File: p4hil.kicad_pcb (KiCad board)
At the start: 4 copper layers, 81.3 x 50.8 mm, 216 parts, among them J1 Conn_02x02_Odd_Even, J10 Conn_01x20, J11 Conn_01x20, J12 Conn_01x20, J13 USB_A_Stacked, J14 Conn_01x04, J15 Conn_01x20, J16 Conn_01x04, J17 Barrel_Jack_Switch, J18 Conn_02x05_Odd_Even, J19 HR871150C, J2 Conn_01x08, J3 USB_C_Receptacle_USB2.0_16P, J4 Conn_01x10, J5 Conn_01x20, J6 Conn_01x20, J7 Conn_01x20, J8 Conn_01x02, J9 Conn_01x06, SW1 SW_Push, SW2 SW_Push, U1 W25Q128JVS, U10 TLV62569DBV, U11 MT9700_SY6280, U3 TLV62569DBV, U4 IPGRI, U6 INA219AxD, U7 CH334F, U8 MT9700_SY6280, U9 MT9700_SY6280, Y1 40MHz(+-10 ppm) C501798, Y2 25Mhz 12pf, Y3 12MHz

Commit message: Swirly gridify
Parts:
- removed R93: 2.2K, Resistor_SMD:R_0402_1005Metric
- added REF**: MountingHole_2.5mm, MountingHole:MountingHole_2.5mm, F.Cu at (177.8, 125.4)
- added REF**: MountingHole_2.5mm, MountingHole:MountingHole_2.5mm, F.Cu at (106.7, 69.5)
- added REF**: MountingHole_2.5mm, MountingHole:MountingHole_2.5mm, F.Cu at (177.8, 69.5)
- added REF**: MountingHole_2.5mm, MountingHole:MountingHole_2.5mm, F.Cu at (106.7, 125.4)
- J10, J11, J12, J15, J6, J7: footprint Connector_PinHeader_2.54mm:PinHeader_1x20_P2.54mm_Vertical -> Connector_PinHeader_2.54mm:PinHeader_1x19_P2.54mm_Vertical
- moved C54 12.3 mm to (182.4, 92.4)
- moved D1 12.3 mm to (184.4, 92.5)
- moved J1 11.8 mm to (165.1, 98.8)
- moved J17 2.81 mm to (176.4, 117.9)
- moved J3 2.81 mm to (182.4, 100.0)
- moved JP3 2.79 mm to (174.0, 103.8), turned to -90 degrees
- moved J10 2.55 mm to (114.3, 100.0)
- moved J11 2.55 mm to (114.3, 105.1)
- moved J12 2.55 mm to (114.3, 95.0)
- moved J15 2.55 mm to (114.3, 107.7)
- moved J6 2.55 mm to (114.3, 97.5)
- moved J7 2.55 mm to (114.3, 102.6)
- moved R85 2.54 mm to (142.2, 110.4)
- moved R88 2.54 mm to (149.9, 110.4)
- moved R92 2.54 mm to (160.0, 110.4)
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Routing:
- net /DeviceUnderTest/T9i: track 0.00 -> 15.0 mm
- net /DeviceUnderTest/T8i: track 0.00 -> 15.0 mm
- net /DeviceUnderTest/T7i: track 0.00 -> 15.0 mm
- net /DeviceUnderTest/T6i: track 0.00 -> 15.0 mm
- net /DeviceUnderTest/T5i: track 0.00 -> 15.0 mm
- net /DeviceUnderTest/T4i: track 0.00 -> 15.0 mm
- net /DeviceUnderTest/T3i: track 0.00 -> 15.0 mm
- net /DeviceUnderTest/T2i: track 0.00 -> 15.0 mm
- net /DeviceUnderTest/T1i: track 0.00 -> 15.0 mm
- net /DeviceUnderTest/T19i: track 0.00 -> 15.0 mm
- net /DeviceUnderTest/T18i: track 0.00 -> 15.0 mm
- net /DeviceUnderTest/T17i: track 0.00 -> 15.0 mm
- net /DeviceUnderTest/T16i: track 0.00 -> 15.0 mm
- net /DeviceUnderTest/T15i: track 0.00 -> 15.0 mm
- net /DeviceUnderTest/T14i: track 0.00 -> 15.0 mm
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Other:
- board size 81.3 x 50.8 mm -> 81.3 x 61 mm
- board text added: "0.5{dblquote}"
- board text added: "0.6{dblquote}"
- board text added: "0.7{dblquote}"
- board text added: "0.8{dblquote}"
- board text added: "0.9{dblquote}"
- board text added: "1.0{dblquote}"
- board text added: "5+x4 swirly grid squares"

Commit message: more routing
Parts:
- C35, C36, C37, C38, C39, C40, R10: moved to F.Cu
- C41, C42, C46, C47, C48, R11, R12, R13, R32, U4, Y2: moved to B.Cu
- R50: value R_Protect -> 1.5k; moved to B.Cu
- moved R34 11.8 mm to (182.3, 72.5)
- moved R13 10.9 mm to (162.4, 78.1), turned to -90 degrees
- moved R32 10.9 mm to (163.4, 78.1), turned to -90 degrees
- moved J18 10.5 mm to (125.7, 79.1), turned to -90 degrees
- moved C41 9.25 mm to (166.7, 87.9), turned to 90 degrees
- moved C42 9.25 mm to (161.4, 87.9), turned to -90 degrees
- moved Y2 9.25 mm to (164.1, 87.9)
- moved C43 8.31 mm to (167.7, 83.3), turned to -90 degrees
- moved C37 7.27 mm to (162.4, 82.3), turned to 0 degrees
- moved R11 7.21 mm to (166.9, 80.0)
- moved R50 7.08 mm to (164.5, 78.1), turned to -90 degrees
- moved SW2 6.78 mm to (105.9, 103.5), turned to -90 degrees
- moved PORT4 5.71 mm to (107.1, 99.6)
- moved R12 4.98 mm to (165.7, 85.6)
- moved C38 4.95 mm to (161.5, 83.6), turned to 0 degrees
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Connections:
- J1 pad 2: /Ethernet/POWER2 -> /Ethernet/POWER1
- J1 pad 3: /Ethernet/POWER1 -> /Ethernet/POWER2
- J2 pad 1: /DeviceUnderTest/T13i -> /DeviceUnderTest/T12i
- J2 pad 2: /DeviceUnderTest/T14i -> /DeviceUnderTest/T13i
- J2 pad 3: /DeviceUnderTest/T15i -> /DeviceUnderTest/T14i
- J2 pad 4: /DeviceUnderTest/T16i -> /DeviceUnderTest/T15i
- J2 pad 5: /DeviceUnderTest/T17i -> /DeviceUnderTest/T16i
- J2 pad 6: /DeviceUnderTest/T18i -> /DeviceUnderTest/T17i
- J2 pad 7: /DeviceUnderTest/T19i -> /DeviceUnderTest/T18i
- J2 pad 8: /DeviceUnderTest/T20i -> /DeviceUnderTest/T19i
- J4 pad 10: /DeviceUnderTest/T10i -> /DeviceUnderTest/T9i
- J4 pad 4: /DeviceUnderTest/T4i -> unconnected-(J4-Pin_4-Pad4)
- J4 pad 5: /DeviceUnderTest/T5i -> /DeviceUnderTest/T4i
- J4 pad 6: /DeviceUnderTest/T6i -> /DeviceUnderTest/T5i
- J4 pad 7: /DeviceUnderTest/T7i -> /DeviceUnderTest/T6i
- J4 pad 8: /DeviceUnderTest/T8i -> /DeviceUnderTest/T7i
- J4 pad 9: /DeviceUnderTest/T9i -> /DeviceUnderTest/T8i
- J8 pad 1: /T11 -> /DeviceUnderTest/T10i
- J8 pad 2: /T12 -> /DeviceUnderTest/T11i
- R50 pad 1: /DeviceUnderTest/T20i -> +3.3V
- R50 pad 2: /T20 -> /MDIO
- U2 pad 10: /T6 -> /T4
- U2 pad 11: /T5 -> /T3
- U2 pad 12: /T4 -> /T2
- U2 pad 13: /T3 -> /T1
- U2 pad 14: /T2 -> /P4/GPIO13/ADC
- U2 pad 15: /T1 -> /B1
- U2 pad 16: /P4/GPIO15/ADC -> /B2
- U2 pad 17: /P4/GPIO16/ADC -> /B3
- U2 pad 18: /P4/GPIO17/ADC -> /B4
- U2 pad 19: /P4/GPIO18/ADC -> /B5
- U2 pad 20: /P4/GPIO19/ADC -> /B6
- U2 pad 22: /P4/GPIO20/ADC -> /B7
- U2 pad 23: /P4/GPIO21/ADC -> /B8
- U2 pad 24: /P4/GPIO22/ADC -> /B9
- U2 pad 25: /P4/GPIO23/ADC -> /B10
- U2 pad 3: /T12 -> /T10
- U2 pad 4: /T11 -> /T9
- U2 pad 5: /T10 -> /T8
- U2 pad 55: /P4/GPIO26/ADC/USB -> /B11
- U2 pad 56: /P4/GPIO27/ADC/USB -> /B12
- U2 pad 57: /P4/GPIO28 -> /B13
- U2 pad 58: /P4/GPIO29 -> /B14
- U2 pad 6: /T9 -> /T7
- U2 pad 60: /P4/GPIO30 -> /T11
- U2 pad 61: /P4/GPIO31 -> /T12
- U2 pad 63: /P4/GPIO32 -> /B15
- U2 pad 64: /P4/GPIO33 -> /B16
- U2 pad 65: /P4/GPIO34 -> /B17
- U2 pad 69: /P4/GPIO37/UART0_TXD -> /B18
- U2 pad 7: /T8 -> /T6
- U2 pad 70: /P4/GPIO38/UART0_RXD -> /B19
- U2 pad 8: /T7 -> /T5
- U2 pad 80: /P4/GPIO39 -> /B20
- U2 pad 92: /T20 -> /PHY_RESETN
- U4 pad 32: /Ethernet/PHY_RESET -> /PHY_RESETN
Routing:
- net +3.3V: track 51.3 -> 180.9 mm, vias 8 -> 13
- net /DeviceUnderTest/I2C_PULL_UP: track 0.00 -> 115.9 mm
- net +5V: track 0.00 -> 107.5 mm
- net /NEOPIXEL_WAKE: track 0.00 -> 61.6 mm, vias 0 -> 1
- net /USB_SERIAL-: track 0.00 -> 55.9 mm, vias 0 -> 4
- net /USB_SERIAL+: track 0.00 -> 55.1 mm, vias 0 -> 2
- net /DeviceUnderTest/B1i: track 3.72 -> 55.9 mm
- net /B20: track 0.00 -> 47.3 mm, vias 0 -> 4
- net /DeviceUnderTest/B2i: track 0.00 -> 46.5 mm
- net /USB Host/USB_VBUS: track 0.00 -> 41.8 mm
- net /DeviceUnderTest/B3i: track 0.00 -> 40.7 mm
- net /MDIO: track 0.00 -> 38.3 mm, vias 0 -> 3
- net /DeviceUnderTest/B4i: track 0.00 -> 35.3 mm
- net /PHY_RESETN: track 0.00 -> 32.1 mm, vias 0 -> 2
- net /DeviceUnderTest/B5i: track 0.00 -> 29.9 mm
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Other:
- board text added: "+V"
- board text added: "1"
- board text added: "2"
- board text added: "3"
- board text added: "4"
- board text added: "45"
- board text added: "5V"
- board text added: "78"
- board text added: "A"
- board text added: "G"
- board text added: "USB"

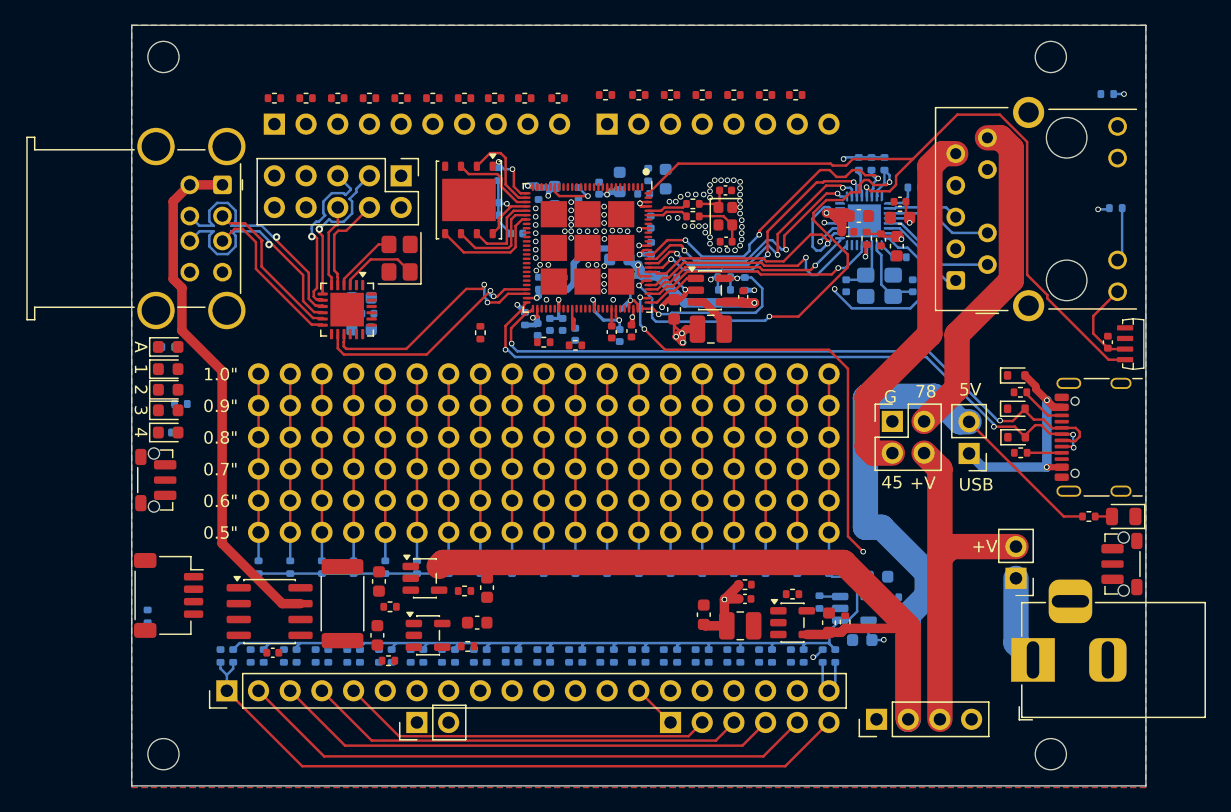
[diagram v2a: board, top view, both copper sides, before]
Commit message: Lots more routing
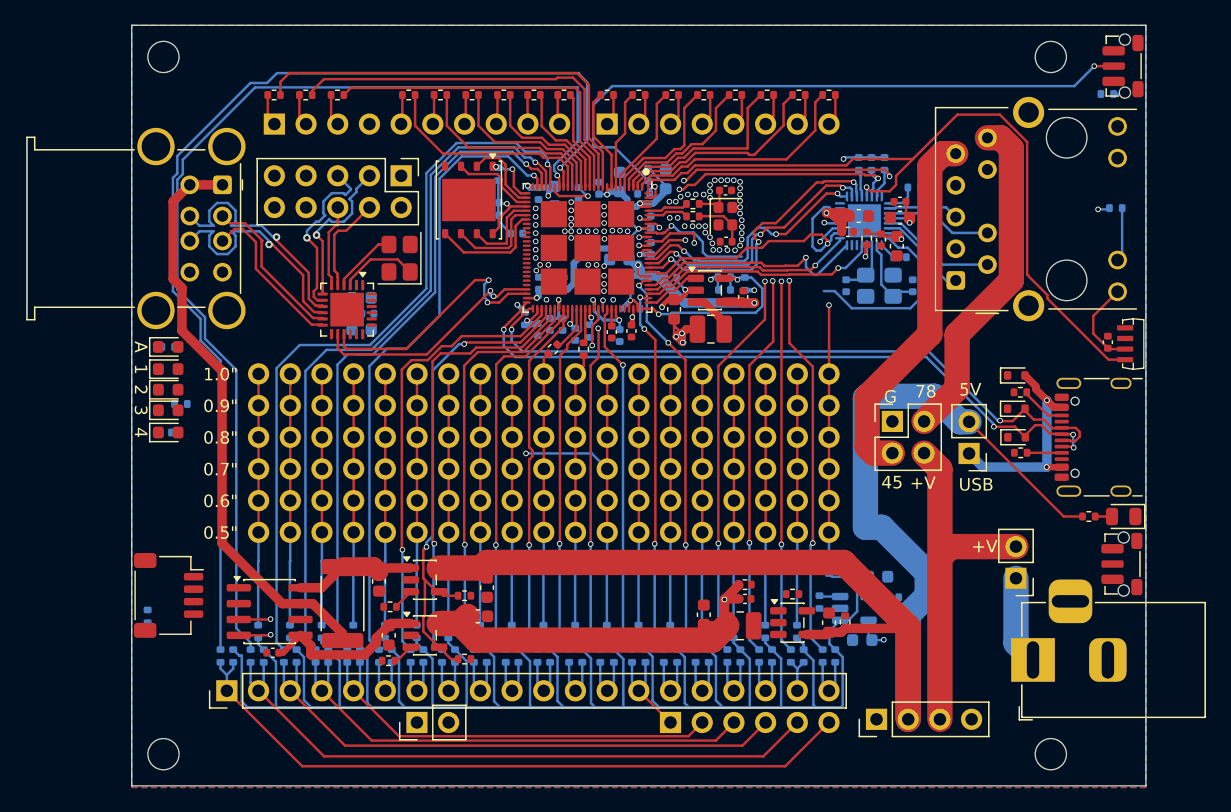
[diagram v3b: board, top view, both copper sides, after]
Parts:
- R24: moved to B.Cu
- moved SW2 84.6 mm to (183.7, 70.3), turned to 90 degrees
- moved R42 20.2 mm to (142.2, 72.6), turned to 180 degrees
- moved R40 20.1 mm to (137.9, 93.0), turned to 45 degrees
- moved R24 8.74 mm to (140.8, 91.5)
- moved R74 5.16 mm to (114.3, 115.6)
- moved R75 5.16 mm to (116.8, 115.6)
- moved R76 5.16 mm to (119.4, 115.6)
- moved R77 5.16 mm to (121.9, 115.6)
- moved R78 5.16 mm to (124.4, 115.6)
- moved R79 5.16 mm to (127.0, 115.6)
- moved R80 5.16 mm to (129.5, 115.6)
- moved R81 5.16 mm to (132.1, 115.6)
- moved R82 5.16 mm to (134.6, 115.6)
- moved R83 5.16 mm to (137.1, 115.6)
- moved R84 5.16 mm to (139.7, 115.6)
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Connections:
- R22 pad 1: /USB Host/POWER_ON -> /USB_POWER_ON
- R23 pad 1: /USB Host/POWER_ON -> /USB_POWER_ON
- U2 pad 1: /T14 -> /T19
- U2 pad 10: /T4 -> /T1
- U2 pad 11: /T3 -> /T2
- U2 pad 12: /T2 -> /T3
- U2 pad 13: /T1 -> /T9
- U2 pad 14: /P4/GPIO13/ADC -> /T8
- U2 pad 15: /B1 -> /T7
- U2 pad 16: /B2 -> /T6
- U2 pad 17: /B3 -> /T5
- U2 pad 18: /B4 -> /T4
- U2 pad 19: /B5 -> /B1
- U2 pad 2: /T13 -> /T18
- U2 pad 20: /B6 -> /B2
- U2 pad 22: /B7 -> /B3
- U2 pad 23: /B8 -> /B4
- U2 pad 24: /B9 -> /B5
- U2 pad 25: /B10 -> /B6
- U2 pad 3: /T10 -> /T17
- U2 pad 4: /T9 -> /T16
- U2 pad 5: /T8 -> /T15
- U2 pad 55: /B11 -> /B7
- U2 pad 56: /B12 -> /USB_POWER_ON
- U2 pad 57: /B13 -> /B8
- U2 pad 58: /B14 -> /B9
- U2 pad 6: /T7 -> /T14
- U2 pad 60: /T11 -> /B10
- U2 pad 61: /T12 -> /B11
- U2 pad 63: /B15 -> /T10
- U2 pad 64: /B16 -> /B12
- U2 pad 65: /B17 -> /T11
- U2 pad 69: /B18 -> /B13
- U2 pad 7: /T6 -> /T13
- U2 pad 70: /B19 -> /B14
- U2 pad 8: /T5 -> /T12
- U2 pad 80: /B20 -> /B15
- U2 pad 84: /MDIO -> /B16
- U2 pad 90: /MDC -> /B19
- U2 pad 92: /PHY_RESETN -> /B17
- U2 pad 93: /T19 -> /B20
- U2 pad 94: /T18 -> /B18
- U2 pad 95: /T17 -> /PHY_RESETN
- U2 pad 97: /T16 -> /MDC
- U2 pad 98: /T15 -> /MDIO
- U8 pad 4: /USB Host/POWER_ON -> /USB_POWER_ON
- U9 pad 4: /USB Host/POWER_ON -> /USB_POWER_ON
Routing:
- net /B1: track 0.00 -> 86.6 mm, vias 0 -> 1
- net /B2: track 0.00 -> 84.9 mm, vias 0 -> 1
- net /DeviceUnderTest/I2C_PULL_UP: track 115.9 -> 180.3 mm
- net /B3: track 0.00 -> 60.3 mm, vias 0 -> 1
- net /B4: track 0.00 -> 56.8 mm, vias 0 -> 1
- net /RESET: track 0.17 -> 54.9 mm, vias 0 -> 2
- net /B5: track 0.00 -> 53.8 mm, vias 0 -> 1
- net /SCL: track 0.00 -> 52.2 mm, vias 0 -> 2
- net /DeviceUnderTest/T12i: track 15.0 -> 66.4 mm, vias 0 -> 1
- net /B6: track 0.00 -> 51.3 mm, vias 0 -> 1
- net /SDA_BOOT: track 0.00 -> 51.2 mm, vias 0 -> 2
- net /B18: track 0.00 -> 43.6 mm, vias 0 -> 3
- net /B17: track 0.00 -> 43.4 mm, vias 0 -> 3
- net /B19: track 0.00 -> 42.5 mm, vias 0 -> 3
- net /USB_POWER_ON: track 0.00 -> 39.8 mm, vias 0 -> 2
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
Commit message: close to routed
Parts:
- R25: moved to F.Cu
- moved R25 5.27 mm to (110.1, 116.9), turned to -90 degrees
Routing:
- net /DeviceUnderTest/T13i: track 22.7 -> 61.5 mm, vias 0 -> 1
- net /DeviceUnderTest/T14i: track 22.7 -> 58.8 mm, vias 0 -> 1
- net /USB Host/SWITCHED_3V3: track 13.5 -> 47.3 mm, vias 0 -> 4
- net +3.3V: track 219.2 -> 252.1 mm, vias 14 -> 17
- net /USB Host/LED4: track 0.00 -> 32.8 mm, vias 0 -> 4
- net /USB Host/LED1: track 0.00 -> 28.0 mm, vias 0 -> 2
- net /DeviceUnderTest/T15i: track 22.7 -> 50.7 mm, vias 0 -> 1
- net /DeviceUnderTest/T16i: track 22.7 -> 47.4 mm, vias 0 -> 1
- net /DeviceUnderTest/T17i: track 22.7 -> 45.1 mm, vias 0 -> 1
- net /USB Host/SWITCHED_5V: track 9.83 -> 31.8 mm, vias 0 -> 2
- net /DeviceUnderTest/T18i: track 22.7 -> 43.7 mm, vias 0 -> 1
- net /USB Host/LED2: track 0.00 -> 20.1 mm, vias 0 -> 4
- net /USB Host/USB_VBUS: track 46.7 -> 65.1 mm
- net /PHY_RESETN: track 24.2 -> 35.2 mm, vias 1 -> 3
- net Net-(U10-FB): track 0.00 -> 6.88 mm
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
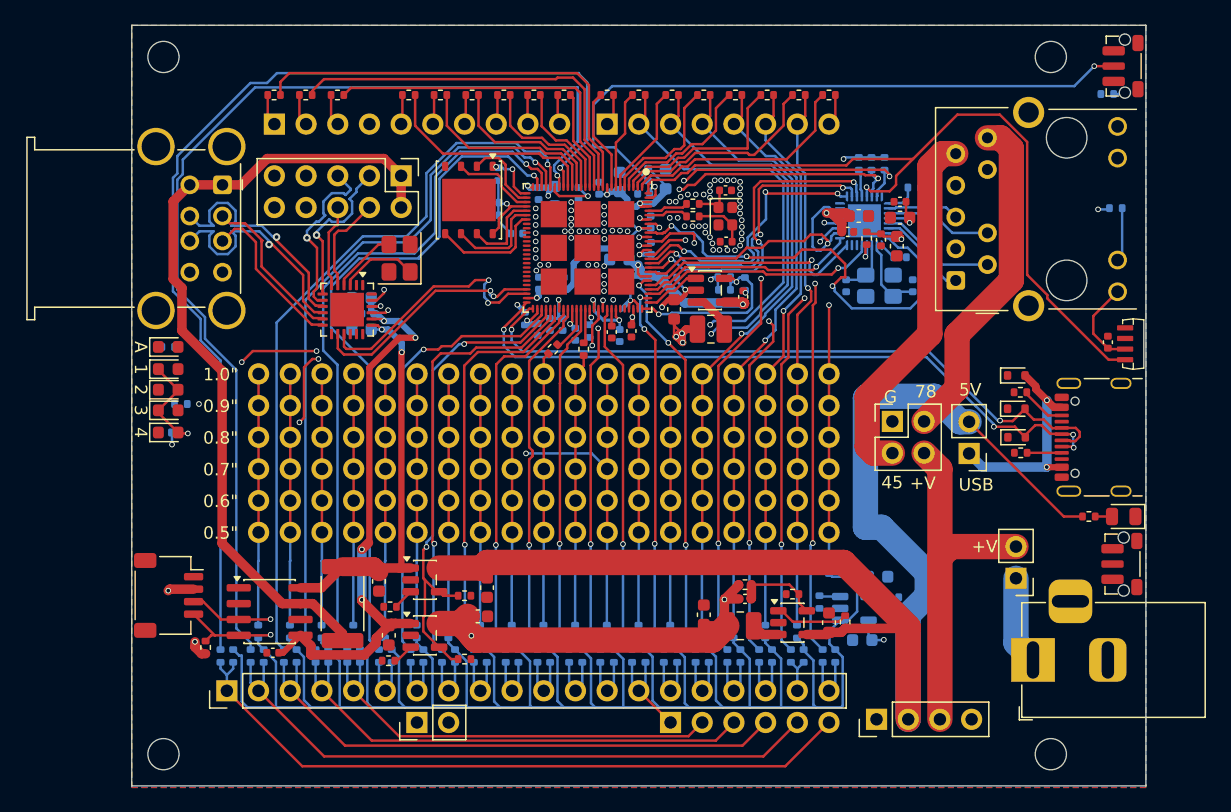
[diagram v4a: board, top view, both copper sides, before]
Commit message: gah, need i2c expander for pull control
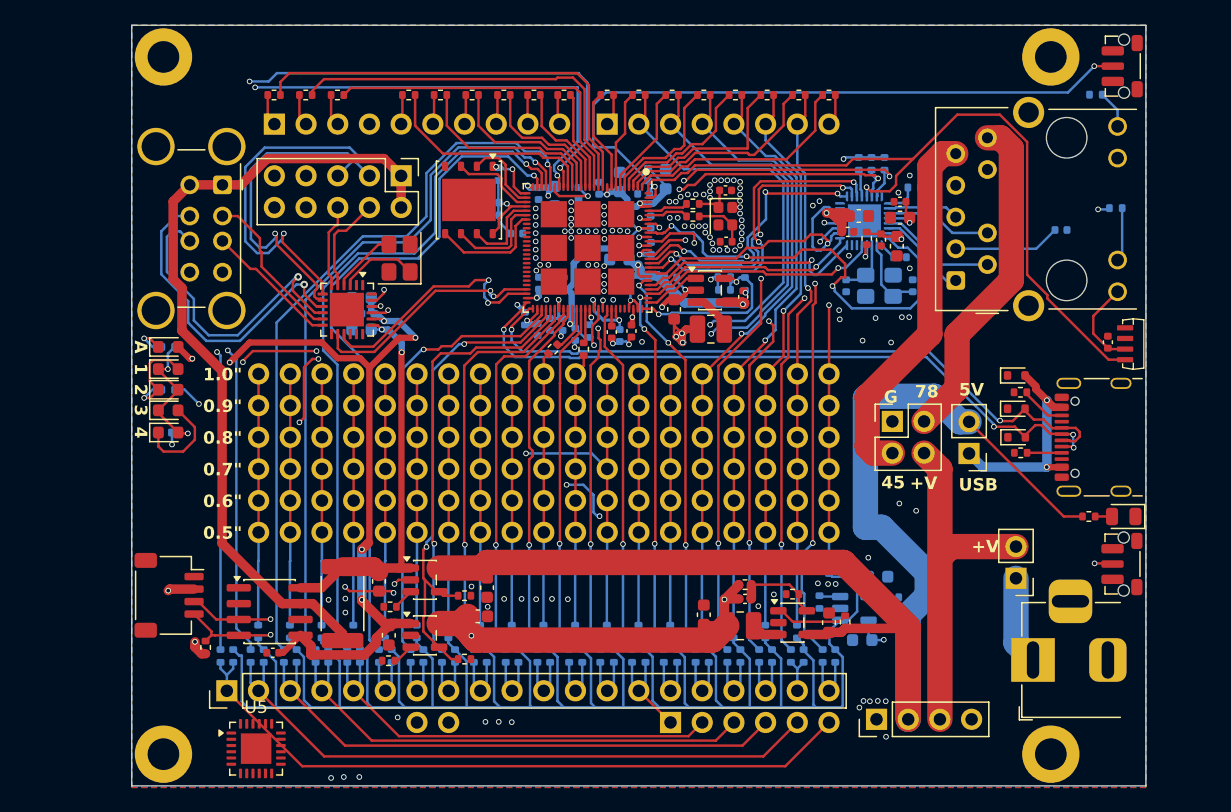
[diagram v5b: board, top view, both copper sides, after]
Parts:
- added U5: PI4IOE5V9535ZDEX, Package_DFN_QFN:VQFN-24-1EP_4x4mm_P0.5mm_EP2.45x2.45mm, F.Cu at (114.1, 125.0)
- REF** (x4): value MountingHole_2.5mm -> MountingHole_2.5mm_Pad; footprint MountingHole:MountingHole_2.5mm -> MountingHole:MountingHole_2.5mm_Pad
- moved C43 10.9 mm to (178.6, 83.4), turned to 0 degrees
- moved R17 1.53 mm to (107.1, 96.2)
- moved R34 0.91 mm to (181.4, 72.6)
- moved SW2 0.07 mm to (183.7, 70.3)
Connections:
- net /DeviceUnderTest/ENABLE_I2C_PULLS renamed /ENABLE_I2C_PULLS
- U2 pad 56: /USB_POWER_ON -> /P4/GPIO27/ADC/USB
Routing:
- net /SDA_BOOT: track 55.4 -> 112.4 mm, vias 2 -> 5
- net /DeviceUnderTest/T11i: track 21.9 -> 42.3 mm
- net /DeviceUnderTest/T10i: track 21.9 -> 42.3 mm
- net /USB Host/SWITCHED_3V3: track 47.3 -> 65.5 mm, vias 4 -> 6
- net /USB Host/D3-: track 12.6 -> 28.4 mm
- net /USB Host/D3+: track 13.9 -> 26.5 mm
- net GND: track 5.13 -> 14.3 mm, vias 76 -> 128
- net /Ethernet/CT: track 0.00 -> 8.58 mm
- net Net-(PORT1-A): track 0.00 -> 8.18 mm, vias 0 -> 1
- net Net-(PORT3-A): track 0.00 -> 7.52 mm
- net /USB Host/D2-: track 19.0 -> 25.4 mm
- net /USB Host/D2+: track 18.9 -> 25.1 mm
- net +3.3V: track 252.1 -> 255.6 mm
- net Net-(ACTIVE1-K): track 0.00 -> 3.13 mm, vias 0 -> 1
- net /USB Host/LED4: track 32.8 -> 35.6 mm, vias 4 -> 5
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
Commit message: clean drc
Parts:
- added C60: 0.1uF, Capacitor_SMD:C_0402_1005Metric, B.Cu at (109.6, 116.2)
- added D9: GREEN LED, Diode_SMD:D_0603_1608Metric, F.Cu at (106.0, 120.3)
- added J20: Conn_02x04_Odd_Even, Connector_PinHeader_2.54mm:PinHeader_2x04_P2.54mm_Vertical, F.Cu at (105.4, 100.0)
- added J21: Conn_01x06, Connector_PinHeader_2.54mm:PinHeader_1x06_P2.54mm_Vertical, F.Cu at (124.5, 126.7)
- added PORT5: LED_Small, LED_SMD:LED_0603_1608Metric, F.Cu at (106.0, 118.4)
- added R73: 470, Resistor_SMD:R_0402_1005Metric, B.Cu at (104.8, 118.3)
- added R93: 2.2K, Resistor_SMD:R_0402_1005Metric, F.Cu at (112.4, 117.8)
- D8: footprint Diode_SMD:D_0805_2012Metric -> Diode_SMD:D_0603_1608Metric
- U5: moved to B.Cu
- moved U5 13.3 mm to (107.5, 113.5), turned to 45 degrees
- moved J16 4.06 mm to (163.8, 126.7)
- moved J13 2.38 mm to (111.4, 77.4)
- moved ACTIVE1 2.29 mm to (107.1, 90.5)
- moved PORT1 2.29 mm to (107.1, 92.3)
- moved PORT2 2.29 mm to (107.1, 93.9)
- moved PORT3 2.29 mm to (107.1, 95.6)
- moved PORT4 2.29 mm to (107.1, 97.4)
- moved R16 2.29 mm to (106.9, 97.4)
- moved R17 2.29 mm to (107.1, 93.9)
- moved R18 2.29 mm to (107.1, 90.5)
- moved J14 0.84 mm to (107.1, 113.5)
- moved D8 0.12 mm to (183.5, 106.4)
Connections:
- U2 pad 56: /P4/GPIO27/ADC/USB -> /USB_POWER_ON
- U5 pad 1: unconnected-(U5-P00-Pad1) -> /P00
- U5 pad 10: /USB_POWER_ON -> /P10
- U5 pad 11: /ENABLE_I2C_PULLS -> /P11
- U5 pad 12: unconnected-(U5-P12-Pad12) -> /P12
- U5 pad 13: unconnected-(U5-P13-Pad13) -> /P13
- U5 pad 14: unconnected-(U5-P14-Pad14) -> /P14
- U5 pad 15: unconnected-(U5-P15-Pad15) -> /P15
- U5 pad 16: unconnected-(U5-P16-Pad16) -> /P16
- U5 pad 17: unconnected-(U5-P17-Pad17) -> /P17
- U5 pad 2: unconnected-(U5-P01-Pad2) -> /P01
- U5 pad 3: unconnected-(U5-P02-Pad3) -> /P02
- U5 pad 4: unconnected-(U5-P03-Pad4) -> /P03
- U5 pad 5: unconnected-(U5-P04-Pad5) -> /P04
- U5 pad 6: unconnected-(U5-P05-Pad6) -> /P05
- U5 pad 7: unconnected-(U5-P06-Pad7) -> /P06
- U5 pad 8: unconnected-(U5-P07-Pad8) -> /ENABLE_I2C_PULLS
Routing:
- net /ENABLE_I2C_PULLS: track 1.43 -> 66.5 mm, vias 0 -> 3
- net GND: track 14.3 -> 38.3 mm, vias 128 -> 181
- net /P00: track 0.00 -> 23.8 mm
- net /P01: track 0.00 -> 21.6 mm
- net /P02: track 0.00 -> 19.9 mm
- net /P03: track 0.00 -> 18.1 mm
- net /P04: track 0.00 -> 16.7 mm
- net /P16: track 0.00 -> 15.8 mm
- net /P05: track 0.00 -> 15.6 mm
- net /P17: track 0.00 -> 14.3 mm
- net /P14: track 0.00 -> 12.3 mm
- net /P15: track 0.00 -> 10.7 mm
- net +5V: track 107.6 -> 116.1 mm
- net /P13: track 0.00 -> 7.16 mm
- net /SCL: track 57.5 -> 64.6 mm, vias 2 -> 3
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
